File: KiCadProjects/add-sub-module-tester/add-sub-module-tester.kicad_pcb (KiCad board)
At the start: 2 copper layers, 91.5 x 68 mm, 18 parts, among them J1 2x4_Connector, J2 1x2_Connector, U1 Toggle_Switch_3PIN, U2 Toggle_Switch_3PIN, U3 Toggle_Switch_3PIN, U4 Toggle_Switch_3PIN

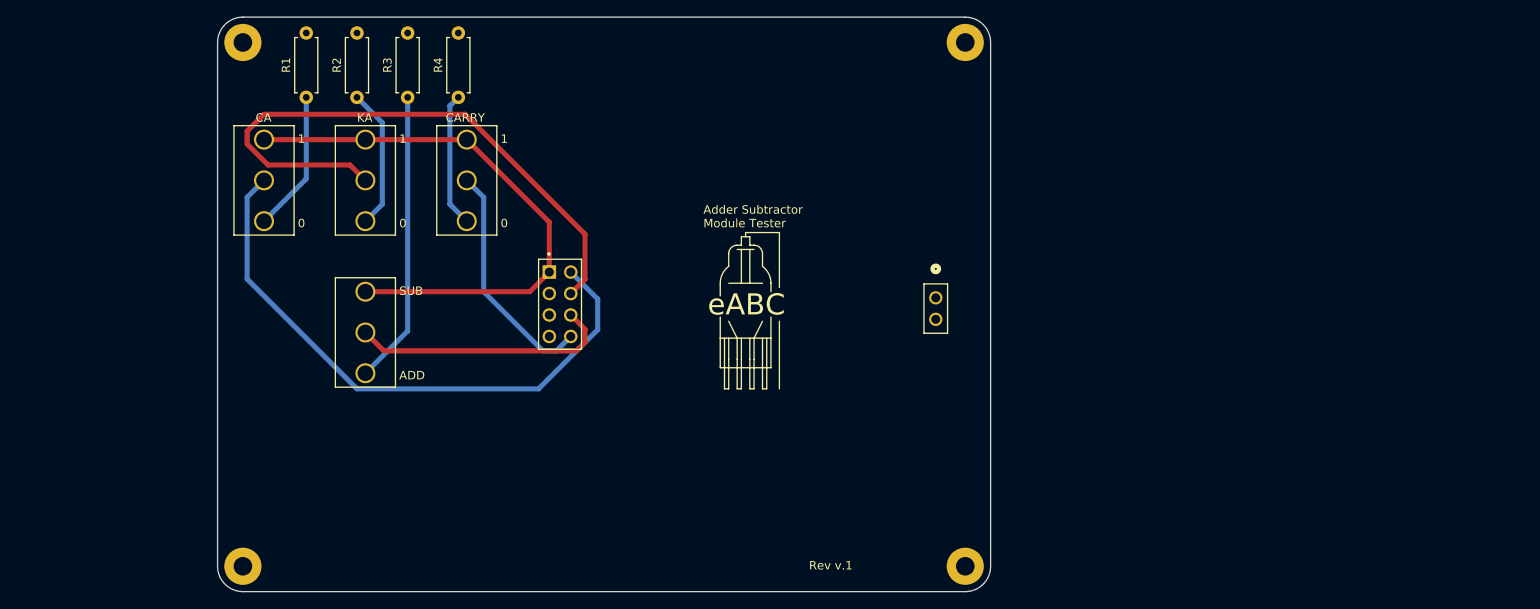
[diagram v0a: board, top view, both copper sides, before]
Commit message: finished tester design
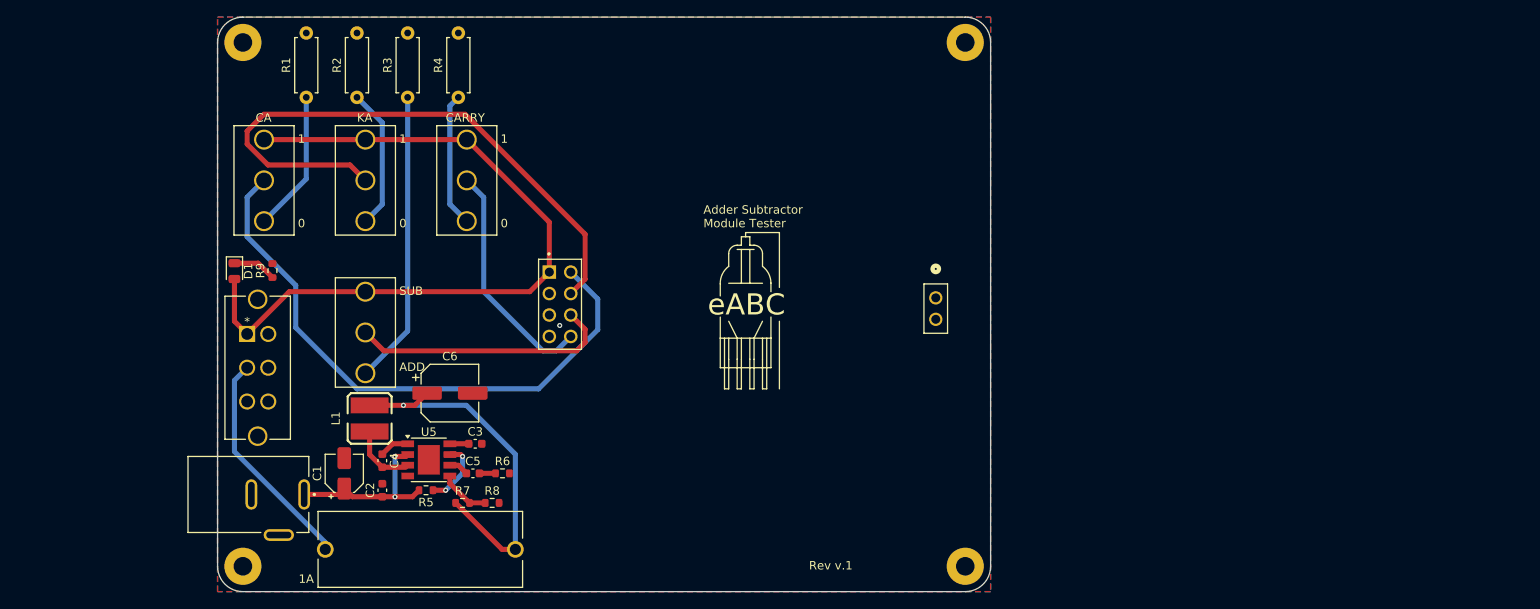
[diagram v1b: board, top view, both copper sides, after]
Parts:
- added C1: 22uF, 0_add_sub_module_tester:CP_Elec_4x5.4, F.Cu at (79.5, 115.5)
- added C2: 0.1uF, 0_add_sub_module_tester:C_0603_1608Metric, F.Cu at (84.0, 117.5)
- added C3: 0.1uF, 0_add_sub_module_tester:C_0603_1608Metric, F.Cu at (95.0, 112.0)
- added C4: 0.1uF, 0_add_sub_module_tester:C_0603_1608Metric, F.Cu at (84.0, 114.0)
- added C5: 6.8nF, 0_add_sub_module_tester:C_0603_1608Metric, F.Cu at (94.7, 115.5)
- added C6: 47uF, 0_add_sub_module_tester:CP_Elec_6.3x7.7, F.Cu at (92.0, 106.0)
- added D1: PWR_Indicator, 0_add_sub_module_tester:LED_0805_2012Metric, F.Cu at (66.5, 91.6)
- added F1: 1A, 0_add_sub_module_tester:Fuse_Holder, F.Cu at (88.5, 124.5)
- added J3: 12V In, 0_add_sub_module_tester:Jack_Connector, F.Cu at (68.5, 118.0)
- added L1: 10uH, 0_add_sub_module_tester:IND-SMD_L4.5-W4.0, F.Cu at (82.5, 109.0)
- added R5: 100k, 0_add_sub_module_tester:R_0603_1608Metric, F.Cu at (89.2, 117.5)
- added R6: 6.8k, 0_add_sub_module_tester:R_0603_1608Metric, F.Cu at (98.2, 115.5)
- added R7: 45.3k, 0_add_sub_module_tester:R_0603_1608Metric, F.Cu at (93.5, 119.0)
- added R8: 10k, 0_add_sub_module_tester:R_0603_1608Metric, F.Cu at (97.0, 119.0)
- added R9: 330, 0_add_sub_module_tester:R_0603_1608Metric, F.Cu at (71.0, 91.5)
- added SW1: PWR_SW, 0_add_sub_module_tester:Slide_Switch_Angled, F.Cu at (68.0, 99.0)
- added U5: AP6503, 0_add_sub_module_tester:AP6503, F.Cu at (89.5, 113.9)
- J1: value 2x4_Connector -> SULLINS_PPTC042LFBN-RC
- J2: value 1x2_Connector -> CONN2_LFBN-RC_SUL
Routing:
- net Net-(C6-Pad1): track 0.00 -> 43.7 mm, vias 0 -> 1
- net Net-(F1-Pad2): track 0.00 -> 26.6 mm
- net +5V: track 66.5 -> 89.6 mm
- net +12V: track 0.00 -> 21.0 mm, vias 0 -> 2
- net /SW: track 0.00 -> 7.95 mm
- net /EN: track 0.00 -> 7.92 mm, vias 0 -> 2
- net /FB: track 0.00 -> 6.00 mm
- net Net-(D1-K): track 0.00 -> 5.20 mm
- net Net-(U5-BST): track 0.00 -> 3.51 mm
- net Net-(U5-COMP): track 0.00 -> 2.35 mm
- net Net-(U5-SS): track 0.00 -> 2.22 mm
- net Net-(C5-Pad2): track 0.00 -> 1.90 mm
- net GND: vias 0 -> 1
- added copper zone on B.Cu, net GND
- added copper zone on F.Cu, net GND

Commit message: still working on tester
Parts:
- J1: value SULLINS_PPTC042LFBN-RC -> 2x4_Connector
- J2: value CONN2_LFBN-RC_SUL -> 1x2_Connector
- U1, U2, U3, U4: footprint 0_add_sub_module_tester:Toggle_Switch_3PIN -> easyeda2kicad:SW-TH_MT-0-103-A101-M200-RS
- moved U1 5.00 mm to (70.0, 81.0)
- moved U2 5.00 mm to (82.0, 81.0)
- moved U3 5.00 mm to (94.0, 81.0)
- moved U4 4.50 mm to (82.0, 98.5)
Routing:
- net +5V: track 89.6 -> 0.00 mm
- net KA: track 71.7 -> 0.00 mm
- net CA: track 70.4 -> 0.00 mm
- net Net-(C6-Pad1): track 43.7 -> 0.00 mm, vias 1 -> 0
- net Net-(R3-Pad1): track 34.7 -> 0.00 mm
- net ADD/SUB: track 32.1 -> 0.00 mm
- net CARRY: track 27.9 -> 0.00 mm
- net Net-(F1-Pad2): track 26.6 -> 0.00 mm
- net +12V: track 21.0 -> 0.00 mm, vias 2 -> 0
- net Net-(R2-Pad1): track 16.7 -> 0.00 mm
- net Net-(R1-Pad1): track 16.7 -> 0.00 mm
- net Net-(R4-Pad1): track 15.9 -> 0.00 mm
- net /SW: track 7.95 -> 0.00 mm
- net /EN: track 7.92 -> 0.00 mm, vias 2 -> 0
- net /FB: track 6.00 -> 0.00 mm
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
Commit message: made some slight adjustments
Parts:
- removed F1: 1A, 0_add_sub_module_tester:Fuse_Holder
- removed R6: 6.8k, 0_add_sub_module_tester:R_0603_1608Metric
- removed R8: 10k, 0_add_sub_module_tester:R_0603_1608Metric
- removed U5: AP6503, 0_add_sub_module_tester:AP6503
- added R3: 100k, Resistor_SMD:R_0603_1608Metric_Pad0.98x0.95mm_HandSolder, F.Cu at (80.9, 120.7)
- added R4: 45.3k, Resistor_SMD:R_0603_1608Metric_Pad0.98x0.95mm_HandSolder, F.Cu at (80.9, 114.9)
- added U1: AP6503, Package_SO:Diodes_SO-8EP, F.Cu at (90.6, 115.5)
- C1: value 22uF -> 0.1uF; footprint 0_add_sub_module_tester:CP_Elec_4x5.4 -> Capacitor_SMD:C_0603_1608Metric_Pad1.08x0.95mm_HandSolder
- C2: value 0.1uF -> 22uF; footprint 0_add_sub_module_tester:C_0603_1608Metric -> Capacitor_SMD:CP_Elec_4x4.5
- C3, C5: footprint 0_add_sub_module_tester:C_0603_1608Metric -> Capacitor_SMD:C_0603_1608Metric_Pad1.08x0.95mm_HandSolder
- C4: value 0.1uF -> 47uF; footprint 0_add_sub_module_tester:C_0603_1608Metric -> Capacitor_SMD:CP_Elec_6.3x7.7
- C6: value 47uF -> 0.1uF; footprint 0_add_sub_module_tester:CP_Elec_6.3x7.7 -> Capacitor_SMD:C_0603_1608Metric_Pad1.08x0.95mm_HandSolder
- J3: footprint 0_add_sub_module_tester:Jack_Connector -> Connector_BarrelJack:BarrelJack_Horizontal
- L1: footprint 0_add_sub_module_tester:IND-SMD_L4.5-W4.0 -> Inductor_SMD:L_Coilcraft_LPS5030
- R5: value 100k -> 10k; footprint 0_add_sub_module_tester:R_0603_1608Metric -> Resistor_SMD:R_0603_1608Metric_Pad0.98x0.95mm_HandSolder
- R7: value 45.3k -> 6.8k; footprint 0_add_sub_module_tester:R_0603_1608Metric -> Resistor_SMD:R_0603_1608Metric_Pad0.98x0.95mm_HandSolder
- SW1: footprint 0_add_sub_module_tester:Slide_Switch_Angled -> easyeda2kicad:SW-TH_SK12D07VG5
- moved C1 17.6 mm to (97.0, 113.6), turned to 180 degrees
- moved C6 16.3 mm to (84.9, 120.7), turned to 180 degrees
- moved R7 12.7 mm to (80.8, 117.8), turned to 180 degrees
- moved C5 10.1 mm to (84.9, 117.8), turned to 180 degrees
- moved L1 9.42 mm to (91.9, 109.2), turned to 180 degrees
- moved C2 8.79 mm to (92.2, 120.7), turned to 180 degrees
- moved J3 6.02 mm to (74.5, 117.5), turned to 0 degrees
- moved R5 4.98 mm to (84.9, 114.9), turned to 0 degrees
- moved C3 4.96 mm to (97.0, 116.5)
- moved C4 4.84 mm to (83.7, 109.2), turned to 180 degrees
- moved SW1 1.41 mm to (67.0, 100.0), turned to -90 degrees
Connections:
- C1 pad 1: +12V -> (no net)
- C1 pad 2: GND -> /SW
- C3 pad 1: Net-(U5-SS) -> +12V
- C4 pad 1: Net-(U5-BST) -> (no net)
- C4 pad 2: /SW -> GND
- C5 pad 1: Net-(U5-COMP) -> (no net)
- L1 pad 2: Net-(C6-Pad1) -> (no net)
- R5 pad 1: /EN -> /FB
- R5 pad 2: +12V -> GND
- R7 pad 1: Net-(C6-Pad1) -> Net-(C5-Pad2)
- R7 pad 2: /FB -> GND
- SW1 pad 1: +5V -> GND
- SW1 pad 2: Net-(F1-Pad2) -> +5V
- SW1 pad 3: unconnected-(SW1-Pad3) -> Net-(C12-Pad1)
- SW1 pad 4: unconnected-(SW1-Pad4) -> GND
- SW1 pad 5: unconnected-(SW1-Pad5) -> GND

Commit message: initial updates after meeting
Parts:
- removed G***: LOGO, 0_add_sub_module_tester:empire
- added C1: 22uF, Capacitor_SMD:CP_Elec_4x4.5, F.Cu at (48.2, 126.0)
- added C2: 0.1uF, Capacitor_SMD:C_0603_1608Metric_Pad1.08x0.95mm_HandSolder, F.Cu at (42.1, 109.6)
- added C3: 0.1uF, Capacitor_SMD:C_0603_1608Metric_Pad1.08x0.95mm_HandSolder, F.Cu at (42.1, 112.1)
- added C4: 0.1uF, Capacitor_SMD:C_0603_1608Metric_Pad1.08x0.95mm_HandSolder, F.Cu at (42.1, 114.6)
- added C5: 6.8nF, Capacitor_SMD:C_0603_1608Metric_Pad1.08x0.95mm_HandSolder, F.Cu at (42.1, 117.1)
- added C6: 47uF, Capacitor_SMD:CP_Elec_6.3x7.7, F.Cu at (49.5, 112.4)
- added L1: 10uH, Inductor_SMD:L_Coilcraft_LPS5030, F.Cu at (55.9, 120.0)
- added R5: 100k, Resistor_SMD:R_0603_1608Metric_Pad0.98x0.95mm_HandSolder, F.Cu at (42.1, 119.6)
- added R6: 6.8k, Resistor_SMD:R_0603_1608Metric_Pad0.98x0.95mm_HandSolder, F.Cu at (42.1, 122.1)
- added R7: 45.3k, Resistor_SMD:R_0603_1608Metric_Pad0.98x0.95mm_HandSolder, F.Cu at (42.1, 124.6)
- added R8: 10k, Resistor_SMD:R_0603_1608Metric_Pad0.98x0.95mm_HandSolder, F.Cu at (42.1, 127.1)
- added U5: AP6503, Package_SO:Diodes_SO-8EP, F.Cu at (48.4, 119.9)
- J1: footprint 0_add_sub_module_tester:2x4_Connector -> Connector_PinSocket_2.54mm:PinSocket_2x04_P2.54mm_Vertical
- J2: footprint 0_add_sub_module_tester:1x2_Connector -> Connector_PinSocket_2.54mm:PinSocket_1x02_P2.54mm_Vertical
- moved J1 2.55 mm to (106.3, 91.7), turned to 0 degrees
- moved J3 0.30 mm to (74.5, 117.8)
- turned J2 to 0 degrees
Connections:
- J3 pad 1: (no net) -> +12V
- J3 pad 2: (no net) -> GND
- J3 pad 3: (no net) -> GND
- SW1 pad 1: GND -> Net-(C6-Pad1)
- SW1 pad 3: Net-(C12-Pad1) -> GND
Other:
- board text added: "Designed by: Peter Hurd"
- board text added: "JLCJLCJLCJLC"
- board text added: "Licensed under CERN-OHL-P v2"
- board text added: "OFF"
- board text added: "ON"
- board text added: "PWR"
- board text added: "Rev. A"
- board text added: "SDMAY25-29"
- board text removed: "JLCSLCSLCS"
- board text removed: "Rev v.1"

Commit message: final updates for Revision A
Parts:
- removed the C1 at (97.0, 113.6)
- removed the C2 at (92.2, 120.7)
- removed the C3 at (97.0, 116.5)
- removed the C4 at (83.7, 109.2)
- removed the C5 at (84.9, 117.8)
- removed the C6 at (84.9, 120.7)
- removed the L1 at (91.9, 109.2)
- removed the R3 at (80.9, 120.7)
- removed the R4 at (80.9, 114.9)
- removed the R5 at (84.9, 114.9)
- removed the R7 at (80.8, 117.8)
- removed the REF** at (153.0, 126.5)
- removed the REF** at (127.0, 95.5)
- removed the REF** at (67.5, 126.5)
- removed the REF** at (153.0, 64.5)
- removed the REF** at (67.5, 64.5)
- removed the REF** at (129.5, 95.5)
- removed the U1 at (90.6, 115.5)
- added H1: MountingHole_Pad, MountingHole:MountingHole_3.2mm_M3_DIN965_Pad, F.Cu at (131.5, 66.0)
- added H2: MountingHole_Pad, MountingHole:MountingHole_3.2mm_M3_DIN965_Pad, F.Cu at (169.5, 66.0)
- added H3: MountingHole_Pad, MountingHole:MountingHole_3.2mm_M3_DIN965_Pad, F.Cu at (214.5, 66.0)
- added H4: MountingHole_Pad, MountingHole:MountingHole_3.2mm_M3_DIN965_Pad, F.Cu at (131.5, 120.0)
- added H5: MountingHole_Pad, MountingHole:MountingHole_3.2mm_M3_DIN965_Pad, F.Cu at (169.5, 120.0)
- added H6: MountingHole_Pad, MountingHole:MountingHole_3.2mm_M3_DIN965_Pad, F.Cu at (214.5, 120.0)
- added J4: Conn_01x02_Socket, Connector_PinSocket_2.54mm:PinSocket_1x02_P2.54mm_Vertical, F.Cu at (216.5, 91.7)
- added Logo1: logo, 0_add_sub_module_tester:logo, F.Cu at (192.0, 87.0)
- added logo2: logo, 0_add_sub_module_tester:logo, B.Cu at (192.0, 87.0)
- C1: footprint Capacitor_SMD:CP_Elec_4x4.5 -> Capacitor_SMD:CP_Elec_5x5.4
- D1: footprint 0_add_sub_module_tester:LED_0805_2012Metric -> LED_SMD:LED_0805_2012Metric_Pad1.15x1.40mm_HandSolder
- J1: value 2x4_Connector -> Conn_01x04_Socket; footprint Connector_PinSocket_2.54mm:PinSocket_2x04_P2.54mm_Vertical -> Connector_PinSocket_2.54mm:PinSocket_1x04_P2.54mm_Vertical
- J2: value 1x2_Connector -> Conn_01x04_Socket; footprint Connector_PinSocket_2.54mm:PinSocket_1x02_P2.54mm_Vertical -> Connector_PinSocket_2.54mm:PinSocket_1x04_P2.54mm_Vertical
- R1, R2, R3, R4: value R -> 330; footprint 0_add_sub_module_tester:R_Axial_DIN0207_L6.3mm_D2.5mm_P7.62mm_Horizontal -> Resistor_THT:R_Axial_DIN0207_L6.3mm_D2.5mm_P7.62mm_Horizontal
- R9: footprint 0_add_sub_module_tester:R_0603_1608Metric -> Resistor_SMD:R_0603_1608Metric_Pad0.98x0.95mm_HandSolder
- moved C2 119.1 mm to (161.1, 116.5)
- moved C4 118.9 mm to (161.1, 113.5), turned to 180 degrees
- moved C1 108.0 mm to (156.1, 121.0), turned to 180 degrees
- moved R8 107.1 mm to (148.6, 115.5)
- moved C3 106.9 mm to (148.6, 121.5), turned to 180 degrees
- moved C5 106.4 mm to (148.6, 118.5), turned to 180 degrees
- moved U5 106.3 mm to (154.6, 115.4), turned to 180 degrees
- moved R7 102.8 mm to (144.6, 115.5)
- moved R6 102.5 mm to (144.6, 118.5), turned to 180 degrees
- moved R5 102.5 mm to (144.6, 121.5), turned to 180 degrees
- moved L1 100.2 mm to (155.6, 109.5), turned to 180 degrees
- moved C6 98.1 mm to (147.6, 109.5), turned to 180 degrees
- moved REF** 76.0 mm to (182.0, 68.2)
- moved J3 63.5 mm to (137.5, 110.0)
- moved D1 63.0 mm to (129.5, 91.6)
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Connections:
- J1 pad 2: CA -> unconnected-(J1-Pin_2-Pad2)
- J1 pad 4: KA -> GND
- J2 pad 1: unconnected-(J2-Pad1) -> CA
- J2 pad 2: unconnected-(J2-Pad2) -> KA
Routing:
- net +5V: track 0.00 -> 98.6 mm
- net GND: track 0.00 -> 47.4 mm, vias 0 -> 4
- net +12V: track 0.00 -> 41.2 mm
- net CA: track 0.00 -> 38.1 mm, vias 0 -> 1
- net Net-(C6-Pad1): track 0.00 -> 36.9 mm
- net ADD/SUB: track 0.00 -> 36.8 mm, vias 0 -> 1
- net Net-(R3-Pad1): track 0.00 -> 36.4 mm
- net KA: track 0.00 -> 23.3 mm
- net Net-(R1-Pad1): track 0.00 -> 16.8 mm
- net Net-(R2-Pad1): track 0.00 -> 16.4 mm
- net Net-(R4-Pad1): track 0.00 -> 15.9 mm
- net CARRY: track 0.00 -> 12.2 mm
- net /EN: track 0.00 -> 10.0 mm
- net /SW: track 0.00 -> 8.67 mm
- net Net-(U5-BST): track 0.00 -> 7.55 mm, vias 0 -> 2
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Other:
- board size 91.5 x 68 mm -> 92 x 63 mm
- board text added: "+5V"
- board text added: "ADD/SUB"
- board text added: "CARRY IN"
- board text added: "CLK"
- board text added: "COUT"
- board text added: "GND"
- board text added: "RST"
- board text added: "SUM"
- board text added: "X/CA"
- board text added: "Y/KA"
